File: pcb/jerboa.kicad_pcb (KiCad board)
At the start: 2 copper layers, 74 parts, among them IC1 SL18860DC, IC2 MAX-M8Q, IC3 Si4460, J1 CONN_01x02, J2 CONN_01x03, J3 CONN_01x02, J4 CONN_01x02, P1 SWD_TC, P2 434, P3 144MHz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

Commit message: More PCB layout
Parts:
- removed C22: 12pF, agg:0402
- removed C24: 6.2pF, agg:0402
- removed L5: 150nH, agg:0402
- removed L8: 56nH, agg:0402
- removed L9: 47nH, agg:0402
- removed U3: BGS12PL6E6327XTSA1, Jerboa:DFN-6-infineon
- added C34: C, agg:0603, F.Cu at (106.5, 91.0)
- added C35: C, agg:0603, F.Cu at (109.7, 82.0)
- added IC4: BGS12AL7, agg:TSLP7-4, F.Cu at (113.5, 88.0)
- added L13: L, agg:0603, F.Cu at (109.6, 91.0)
- added L14: L, agg:0603, F.Cu at (106.5, 82.0)
- L2: value 390nH -> 250nH
- L3: value 220nH -> 100nH
- L4: footprint agg:0402 -> agg:0603
- P2: value 434 -> 434MHz
- moved C9 129.8 mm to (119.2, 86.6)
- moved R5 129.5 mm to (114.2, 85.8), turned to 270 degrees
- moved R4 128.1 mm to (115.9, 85.6), turned to 180 degrees
- moved R2 123.8 mm to (114.2, 79.1), turned to 180 degrees
- moved C6 122.7 mm to (127.0, 88.7), turned to 180 degrees
- moved C4 122.5 mm to (117.9, 81.7), turned to 180 degrees
- moved C2 121.9 mm to (116.1, 81.3), turned to 270 degrees
- moved C10 121.5 mm to (119.0, 84.1), turned to 180 degrees
- moved J1 120.2 mm to (103.2, 87.0), turned to 90 degrees
- moved R1 118.7 mm to (116.3, 79.1)
- moved C1 115.5 mm to (114.0, 83.5), turned to 90 degrees
- moved C8 114.2 mm to (120.9, 81.6)
- moved R8 111.9 mm to (123.0, 78.5), turned to 180 degrees
- moved C3 110.5 mm to (117.9, 80.3), turned to 180 degrees
- moved Y1 109.1 mm to (114.4, 81.2), turned to 90 degrees
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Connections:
- D2 pad 1: Net-(C30-Pad1) -> Net-(D2-Pad1)
- D3 pad 1: Net-(C33-Pad2) -> Net-(D3-Pad1)
- IC3 pad 2: /radio/RADIO_RXp -> GND
- IC3 pad 3: /radio/RADIO_RXn -> GND
- J2 pad 1: /I2C_SCL -> /WSPR_ENABLE
- J2 pad 2: /I2C_SDA -> /I2C_SCL
- J2 pad 3: /WSPR_ENABLE -> /I2C_SDA
- L3 pad 1: /radio/RADIO_RXn -> Net-(C26-Pad1)
- L3 pad 2: /radio/RADIO_RXp -> Net-(C28-Pad1)
- P2 pad 1: Net-(C30-Pad1) -> Net-(D2-Pad1)
- P3 pad 1: Net-(C33-Pad2) -> Net-(D3-Pad1)
- U1 pad 16: Net-(U1-Pad16) -> /GPS_~RESET
- U1 pad 18: /GPS_~RESET -> Net-(U1-Pad18)
- U1 pad 7: /FREQ_CTRL -> /MCU_SHUTDOWN_TO_RADIO
- U1 pad 8: /MCU_SHUTDOWN_TO_RADIO -> /FREQ_CTRL
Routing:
- net 3v3: track 0.00 -> 79.4 mm, vias 0 -> 4
- net GND: track 3.78 -> 67.4 mm, vias 0 -> 15
- net /NRST: track 0.00 -> 24.6 mm, vias 0 -> 4
- net /SWDIO: track 0.00 -> 9.32 mm
- net /GPS_~RESET: track 0.00 -> 8.83 mm
- net /FREQ_CTRL: track 0.00 -> 8.43 mm, vias 0 -> 2
- net /SWCLK: track 0.00 -> 7.84 mm
- net /MCU_SHUTDOWN_TO_RADIO: track 0.00 -> 7.44 mm, vias 0 -> 2
- net /MCU_nIRQ_TO_RADIO: track 0.00 -> 6.45 mm, vias 0 -> 2
- net /MCU_SCK: track 0.00 -> 6.27 mm
- net /WSPR_ENABLE: track 0.00 -> 6.11 mm
- net /MCU_MOSI: track 0.00 -> 6.02 mm, vias 0 -> 2
- net /I2C_SCL: track 0.00 -> 5.82 mm
- net /SOLAR_CELL_VOLTAGE: track 0.00 -> 5.56 mm
- net /MCU_MISO: track 0.00 -> 5.45 mm, vias 0 -> 2
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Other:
- board outline added: 44.6 x 17.8 mm
- board text added: "?"

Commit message: More pcb routing
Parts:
- C10, C7, C8, C9, L1: moved to B.Cu
- R6: footprint agg:0402 -> agg:0603
- moved R9 51.8 mm to (113.3, 89.4), turned to 180 degrees
- moved C14 36.8 mm to (127.0, 91.1)
- moved D1 35.9 mm to (117.2, 78.9)
- moved C11 28.9 mm to (135.5, 78.4)
- moved R6 25.8 mm to (120.3, 78.9), turned to 180 degrees
- moved C12 14.3 mm to (142.9, 78.3), turned to 180 degrees
- moved C13 13.6 mm to (145.0, 79.3)
- moved C15 12.1 mm to (138.8, 83.1), turned to 180 degrees
- moved L6 9.46 mm to (114.6, 99.2), turned to 270 degrees
- moved C23 9.35 mm to (113.1, 99.3), turned to 0 degrees
- moved J3 9.13 mm to (147.6, 81.9), turned to 90 degrees
- moved C33 8.01 mm to (106.5, 97.6)
- moved C26 7.62 mm to (112.0, 96.7)
- moved C35 5.74 mm to (104.2, 83.6), turned to 180 degrees
- moved D2 4.56 mm to (109.7, 82.2)
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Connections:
- U1 pad 7: /MCU_SHUTDOWN_TO_RADIO -> /FREQ_CTRL
- U1 pad 8: /FREQ_CTRL -> /MCU_SHUTDOWN_TO_RADIO
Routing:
- net GND: track 67.4 -> 141.5 mm, vias 15 -> 28
- net 3v3: track 79.4 -> 114.2 mm
- net Net-(C12-Pad1): track 0.00 -> 18.8 mm, vias 0 -> 1
- net Net-(R6-Pad1): track 0.00 -> 4.76 mm
- net /NRST: track 24.6 -> 21.3 mm
- net Net-(C25-Pad1): track 3.24 -> 0.00 mm
- net Net-(L1-Pad2): track 0.00 -> 3.09 mm, vias 0 -> 1
- net /FREQ_CTRL: track 8.43 -> 5.62 mm
- net Net-(C26-Pad1): track 2.42 -> 0.00 mm
- net Net-(AE1-Pad2): track 0.00 -> 2.35 mm
- net /MCU_CLK: track 5.04 -> 2.71 mm
- net /SI4460_CLK: track 1.39 -> 3.71 mm
- net /BATT_V: track 4.20 -> 6.33 mm
- net /GPS_~RESET: track 8.83 -> 10.8 mm, vias 0 -> 2
- net Net-(C20-Pad2): track 1.99 -> 0.00 mm
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- added copper zone on B.Cu, net GND
- added copper zone on F.Cu, net GND
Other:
- board size 44.6 x 17.8 mm -> 47.8 x 19.3 mm

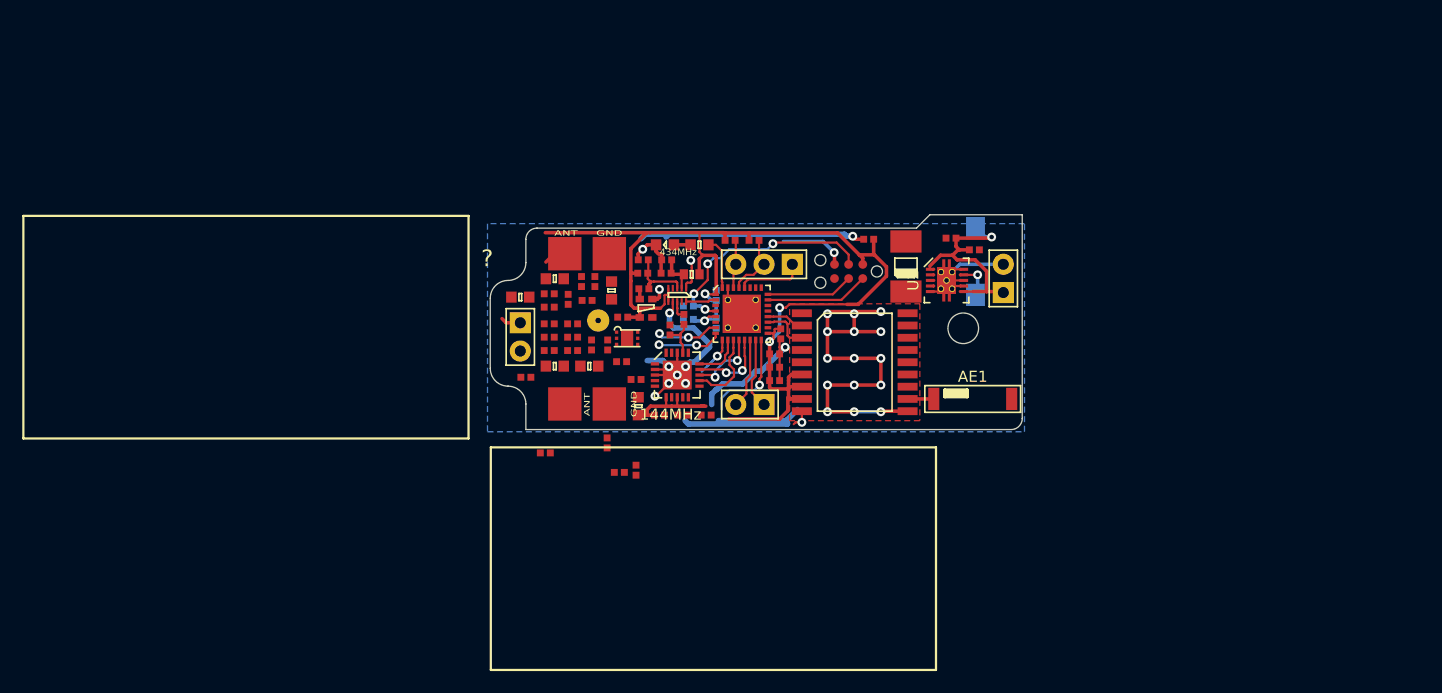
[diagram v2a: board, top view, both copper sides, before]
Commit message: Restart routing, attempt to preserve ground plane this time
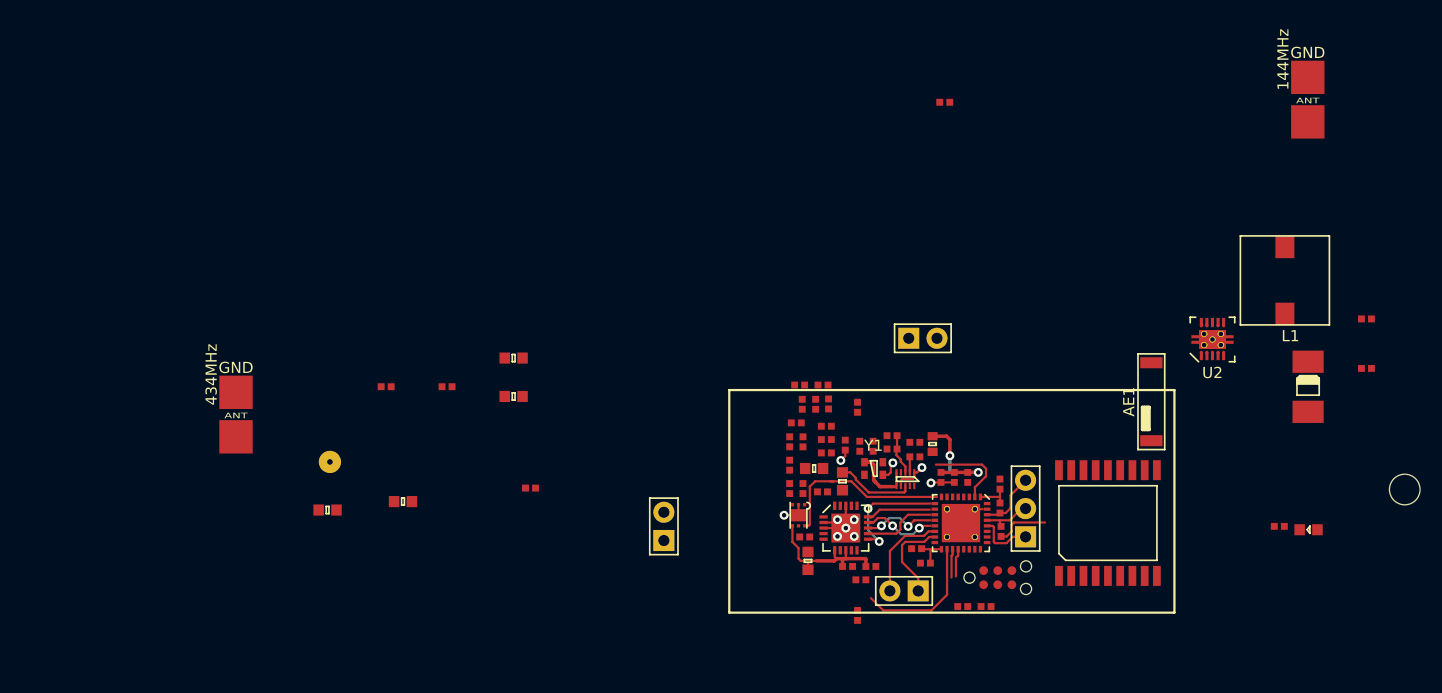
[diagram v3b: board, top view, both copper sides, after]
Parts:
- C10, C7, C8, C9, L1: moved to F.Cu
- R4: footprint agg:0402 -> agg:0603
- R6: footprint agg:0603 -> agg:0402
- moved P3 70.3 mm to (175.0, 65.9), turned to 0 degrees
- moved D1 63.2 mm to (175.0, 104.5)
- moved R6 57.9 mm to (172.4, 104.2), turned to 0 degrees
- moved C14 53.2 mm to (180.2, 90.0)
- moved X1 42.2 mm to (183.7, 100.9)
- moved C12 38.0 mm to (180.2, 85.6), turned to 0 degrees
- moved C15 36.7 mm to (175.0, 89.4), turned to 0 degrees
- moved P2 34.7 mm to (78.7, 94.2), turned to 0 degrees
- moved C11 34.6 mm to (146.1, 111.4), turned to 180 degrees
- moved R7 34.3 mm to (147.4, 104.7), turned to 270 degrees
- moved R8 34.2 mm to (147.3, 102.5), turned to 90 degrees
- moved J2 32.2 mm to (149.6, 102.6), turned to 90 degrees
- moved R9 31.1 mm to (134.5, 112.2), turned to 270 degrees
- moved P1 30.6 mm to (147.1, 108.8), turned to 0 degrees
- moved C30 29.5 mm to (134.5, 93.5), turned to 270 degrees
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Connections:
- U1 pad 16: /GPS_~RESET -> Net-(U1-Pad16)
- U1 pad 18: Net-(U1-Pad18) -> /MCU_SHUTDOWN_TO_RADIO
- U1 pad 21: Net-(U1-Pad21) -> /GPS_~RESET
- U1 pad 7: /FREQ_CTRL -> Net-(U1-Pad7)
- U1 pad 8: /MCU_SHUTDOWN_TO_RADIO -> /FREQ_CTRL
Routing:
- net GND: track 141.5 -> 26.6 mm, vias 28 -> 10
- net 3v3: track 114.2 -> 36.1 mm, vias 4 -> 2
- net /NRST: track 21.3 -> 0.00 mm, vias 4 -> 0
- net Net-(C12-Pad1): track 18.8 -> 0.00 mm, vias 1 -> 0
- net /GPS_~RESET: track 10.8 -> 0.00 mm, vias 2 -> 0
- net /FREQ_CTRL: track 5.62 -> 16.4 mm, vias 2 -> 0
- net /SWDIO: track 9.32 -> 0.00 mm
- net /SWCLK: track 7.84 -> 0.00 mm
- net /MCU_SHUTDOWN_TO_RADIO: track 5.82 -> 12.0 mm, vias 2 -> 0
- net /MCU_nIRQ_TO_RADIO: track 4.89 -> 10.2 mm, vias 1 -> 2
- net Net-(IC1-Pad8): track 1.70 -> 7.02 mm
- net /MCU_CLK: track 2.71 -> 7.62 mm
- net Net-(R6-Pad1): track 4.76 -> 0.00 mm
- net /SI4460_CLK: track 3.71 -> 0.00 mm
- net Net-(L1-Pad2): track 3.09 -> 0.00 mm, vias 1 -> 0
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- removed copper zone on B.Cu, net GND
- removed copper zone on F.Cu, net GND
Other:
- board outline removed
- board text removed: "?"

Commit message: Begin routing pcb (again)
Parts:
- removed C15: 100uF, Jerboa:avx_2312
- removed R5: 10k, agg:0402
- added U3: NCP4620, agg:SC-70-5, F.Cu at (137.2, 96.5)
- C1: value 100nF -> 10uF
- C13: value 100nF -> 10nF
- C14: value 2.2uF -> 100pF
- C2: value 22nF -> 470pF
- C3: value 10uF -> 1uF
- C4: value 100nF -> 1uF
- IC1: value SL18860DC -> ADP1607; footprint agg:DFN-10-SL18860DC -> Jerboa:LFCSP-2x2
- L1: value 6.8uH -> 2.2uH; footprint Jerboa:wurth_7447789006 -> Jerboa:0806
- R1: value 10k -> 953k
- R2: value 10k -> 620k
- R3: value 50 -> 470k; footprint agg:0603-L -> agg:0402
- R4: value 10k -> 4k7; footprint agg:0603 -> agg:0402
- U2: value TPS61025DRCR -> FDC6329L; footprint Jerboa:VSON-10 -> Jerboa:SuperSOT-6
- Y1: footprint Jerboa:2x1.6mm_TCXO -> agg:TG-5006CG
- moved AE1 43.1 mm to (137.0, 128.9), turned to 90 degrees
- moved U2 34.4 mm to (132.1, 85.1)
- moved R4 26.7 mm to (125.7, 74.5)
- moved R3 26.5 mm to (130.8, 72.4)
- moved C2 26.1 mm to (129.5, 72.4)
- moved IC2 22.0 mm to (140.3, 118.2), turned to 270 degrees
- moved R1 17.5 mm to (151.1, 88.5)
- moved IC1 15.7 mm to (148.6, 87.6)
- moved C1 13.2 mm to (144.8, 88.5)
- moved R2 13.2 mm to (149.4, 90.2)
- moved C16 11.8 mm to (132.7, 115.0)
- moved P1 9.50 mm to (154.7, 114.5)
- moved C11 9.50 mm to (153.7, 117.1)
- moved R9 3.94 mm to (131.0, 110.4)
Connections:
- C1 pad 1: GND -> 3v3
- C1 pad 2: 3v3 -> GND
- C13 pad 1: Net-(C12-Pad1) -> GND
- C13 pad 2: GND -> 1v8
- C14 pad 1: 3v3 -> Net-(C14-Pad1)
- C14 pad 2: GND -> Net-(C14-Pad2)
- C17 pad 2: 3v3 -> 3v3_switched
- C18 pad 2: 3v3 -> 3v3_switched
- C19 pad 2: 3v3 -> 3v3_switched
- C2 pad 2: Net-(C2-Pad2) -> 3v3_switched
- C3 pad 2: Net-(C3-Pad2) -> 3v3_switched
- C4 pad 1: GND -> 1v8
- C4 pad 2: Net-(C3-Pad2) -> GND
- IC1 pad 1: GND -> Net-(C12-Pad1)
- IC1 pad 2: Net-(C3-Pad2) -> Net-(C12-Pad1)
- IC1 pad 3: Net-(C2-Pad2) -> Net-(IC1-Pad3)
- IC1 pad 4: Net-(IC1-Pad4) -> GND
- IC1 pad 5: 3v3 -> Net-(IC1-Pad5)
- IC3 pad 17: /SI4460_CLK -> Net-(C14-Pad2)
- IC3 pad 6: 3v3 -> 3v3_switched
- IC3 pad 8: 3v3 -> 3v3_switched
- IC4 pad 4: 3v3 -> 3v3_switched
- L1 pad 2: Net-(L1-Pad2) -> Net-(IC1-Pad5)
- L2 pad 1: 3v3 -> 3v3_switched
- R1 pad 2: Net-(C2-Pad2) -> Net-(IC1-Pad3)
- R2 pad 1: Net-(C2-Pad2) -> Net-(IC1-Pad3)
- R3 pad 1: 3v3 -> Net-(C2-Pad1)
- R3 pad 2: Net-(C3-Pad2) -> 3v3
- R4 pad 1: Net-(IC1-Pad8) -> Net-(R4-Pad1)
- R4 pad 2: /SI4460_CLK -> GND
- U1 pad 2: /MCU_CLK -> GND
- U1 pad 7: Net-(U1-Pad7) -> /RADIO_PWR_EN
- U2 pad 1: Net-(C12-Pad1) -> Net-(R4-Pad1)
- U2 pad 2: 3v3 -> 3v3_switched
- U2 pad 3: Net-(U2-Pad3) -> 3v3_switched
- U2 pad 4: Net-(U2-Pad4) -> 3v3
- U2 pad 5: GND -> /RADIO_PWR_EN
- U2 pad 6: Net-(C12-Pad1) -> Net-(C2-Pad1)
- Y1 pad 3: Net-(C2-Pad1) -> Net-(C14-Pad1)
- Y1 pad 4: 3v3 -> 1v8
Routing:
- net 3v3: track 36.1 -> 17.0 mm
- net /MCU_SHUTDOWN_TO_RADIO: track 12.0 -> 0.00 mm
- net /BATT_V: track 8.35 -> 0.00 mm
- net /SOLAR_CELL_VOLTAGE: track 7.96 -> 0.00 mm
- net /MCU_CLK: track 7.62 -> 0.00 mm
- net Net-(IC1-Pad8): track 7.02 -> 0.00 mm
- net 3v3_switched: track 0.00 -> 5.62 mm
- net Net-(C2-Pad2): track 3.48 -> 0.00 mm
- net GND: track 26.6 -> 29.2 mm, vias 10 -> 8
- net Net-(AE1-Pad2): track 0.00 -> 2.45 mm
- net Net-(C3-Pad2): track 1.15 -> 0.00 mm

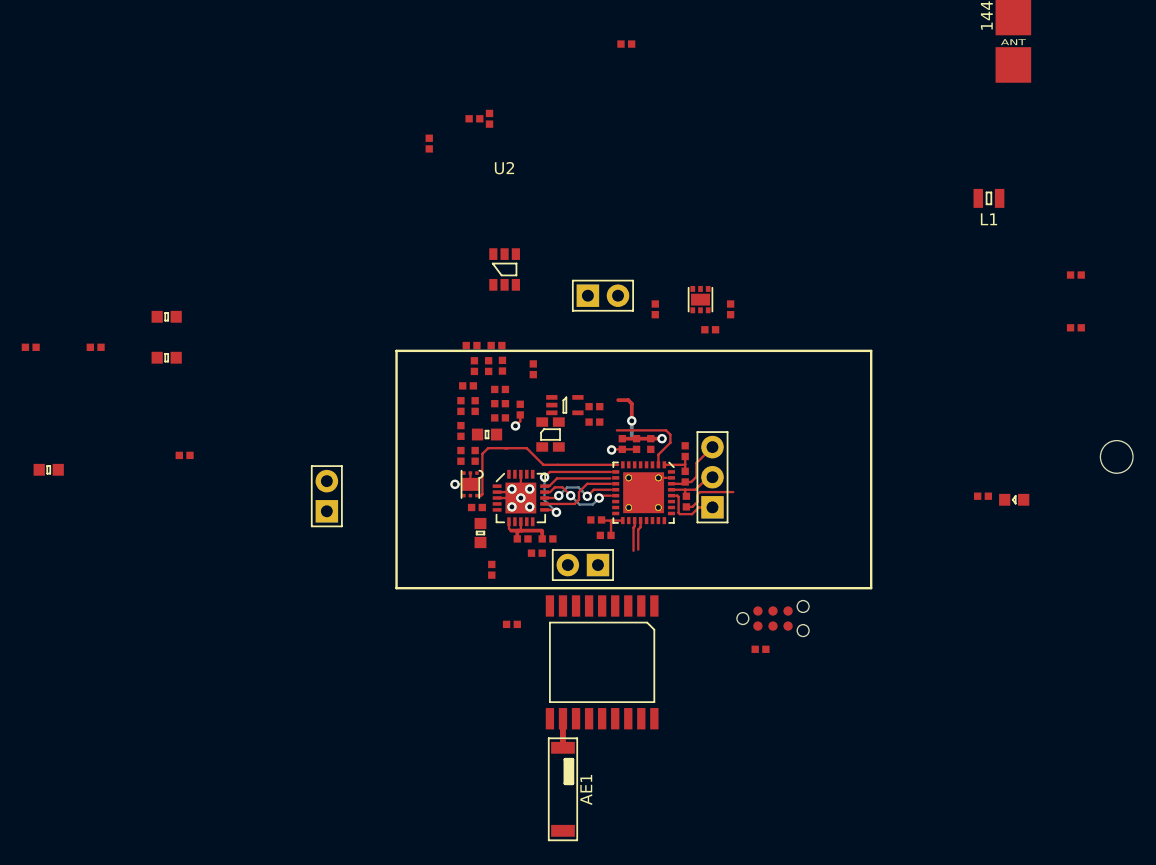
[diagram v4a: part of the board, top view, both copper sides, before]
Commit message: WIP: rough component layout for PCB
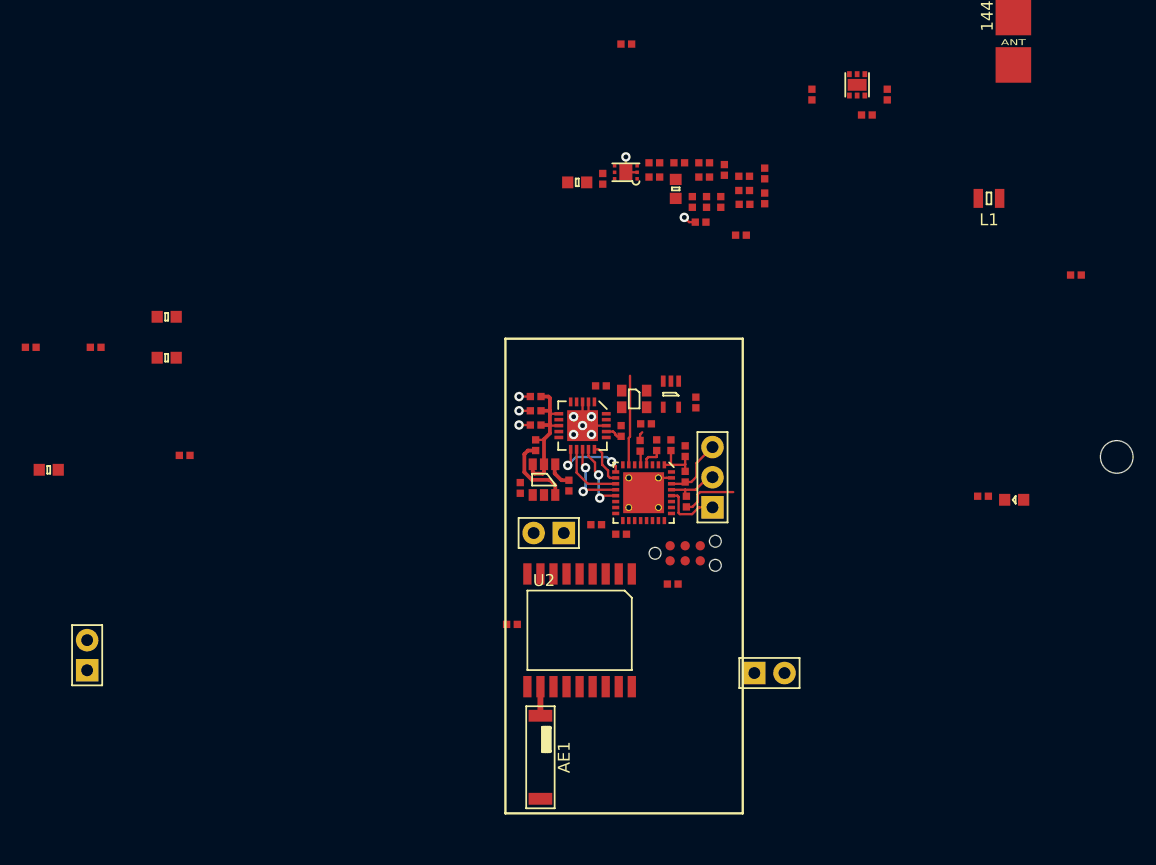
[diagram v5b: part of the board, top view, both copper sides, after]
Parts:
- moved C14 39.3 mm to (141.9, 98.7), turned to 270 degrees
- moved J3 34.8 mm to (154.4, 119.1)
- moved R3 31.2 mm to (133.4, 103.5)
- moved R4 31.1 mm to (137.5, 103.3)
- moved L2 30.7 mm to (138.2, 77.8), turned to 0 degrees
- moved C20 29.7 mm to (140.3, 77.5), turned to 90 degrees
- moved C23 29.6 mm to (144.7, 76.1), turned to 0 degrees
- moved IC4 29.4 mm to (142.3, 76.9), turned to 180 degrees
- moved L6 29.1 mm to (146.8, 76.1), turned to 0 degrees
- moved C26 29.0 mm to (148.9, 76.1), turned to 0 degrees
- moved C33 28.6 mm to (154.0, 77.0), turned to 90 degrees
- moved C28 28.2 mm to (150.6, 76.7), turned to 90 degrees
- moved C2 28.0 mm to (134.7, 99.9), turned to 90 degrees
- moved C21 27.9 mm to (144.7, 77.3), turned to 0 degrees
- moved C29 27.8 mm to (152.3, 77.2), turned to 0 degrees
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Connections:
- U1 pad 16: Net-(U1-Pad16) -> /RADIO_PWR_EN
- U1 pad 18: /MCU_SHUTDOWN_TO_RADIO -> Net-(U1-Pad18)
- U1 pad 7: /RADIO_PWR_EN -> /MCU_SHUTDOWN_TO_RADIO
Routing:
- net /FREQ_CTRL: track 16.4 -> 0.00 mm
- net /MCU_SHUTDOWN_TO_RADIO: track 0.00 -> 7.55 mm
- net 3v3_switched: track 5.62 -> 12.7 mm
- net GND: track 29.2 -> 22.2 mm, vias 8 -> 10
- net 3v3: track 17.0 -> 10.3 mm, vias 2 -> 0
- net Net-(C2-Pad1): track 0.00 -> 6.48 mm
- net /MCU_nIRQ_TO_RADIO: track 10.2 -> 6.60 mm
- net /TX_GPS_from_MCU: track 2.59 -> 0.00 mm
- net /RX_GPS_from_MCU: track 2.53 -> 0.00 mm
- net Net-(R4-Pad1): track 0.00 -> 2.23 mm
- net /SI4460_NSS: track 5.82 -> 3.64 mm
- net /NRST: track 0.00 -> 1.95 mm
- net Net-(C14-Pad2): track 0.00 -> 1.46 mm
- net /MCU_SCK: track 6.67 -> 5.65 mm
- net /MCU_MOSI: track 6.67 -> 5.92 mm

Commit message: WIP: More PCB routing
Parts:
- moved J1 57.9 mm to (154.7, 115.0)
- moved P2 56.3 mm to (134.6, 88.1), turned to 180 degrees
- moved R1 52.5 mm to (146.2, 119.6), turned to 180 degrees
- moved R2 50.8 mm to (146.8, 120.3), turned to 270 degrees
- moved X1 48.9 mm to (142.3, 127.0)
- moved IC1 48.0 mm to (147.2, 115.3), turned to 90 degrees
- moved C1 46.4 mm to (145.5, 115.0)
- moved C12 46.2 mm to (146.5, 117.2), turned to 180 degrees
- moved L1 44.0 mm to (149.3, 116.2), turned to 90 degrees
- moved P3 35.9 mm to (150.2, 91.8)
- moved L2 17.1 mm to (137.4, 94.8)
- moved IC4 16.1 mm to (139.8, 92.8)
- moved C20 15.8 mm to (137.8, 93.0)
- moved C21 11.0 mm to (154.8, 81.7)
- moved C23 11.0 mm to (154.8, 80.5)
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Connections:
- U1 pad 7: /MCU_SHUTDOWN_TO_RADIO -> /FREQ_CTRL
- U1 pad 8: /FREQ_CTRL -> /MCU_SHUTDOWN_TO_RADIO
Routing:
- net /FREQ_CTRL: track 0.00 -> 12.2 mm
- net 3v3: track 10.3 -> 21.3 mm
- net GND: track 22.2 -> 28.5 mm, vias 10 -> 14
- net 3v3_switched: track 12.7 -> 17.6 mm
- net /MCU_SHUTDOWN_TO_RADIO: track 7.55 -> 12.2 mm
- net 1v8: track 0.00 -> 2.98 mm
- net Net-(R4-Pad1): track 2.23 -> 0.00 mm
- net Net-(C14-Pad1): track 0.00 -> 1.57 mm
- net Net-(C20-Pad1): track 0.00 -> 1.47 mm
- net Net-(C2-Pad1): track 6.48 -> 5.19 mm
- net Net-(C20-Pad2): track 0.00 -> 1.15 mm
